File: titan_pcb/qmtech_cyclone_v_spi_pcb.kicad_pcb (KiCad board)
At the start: 2 copper layers, 146.1 x 95 mm, 47 parts, among them J1 FPGA, J10 OLED_CONN, J11 OLED_CONN, J12 CH341_PRG_CONN, J13 SPI_HEADER, J14 SPI_HEADER, J15 I2C_PULLUP, J16 I2C_PULLUP, J17 I2C_PULLUP, J18 I2C_PULLUP, J19 Barrel_Jack_MountingPin, J2 FPGA, J20 PWR_SW, J21 PWR_SW, J22 PWR_SW, J23 PWR_SW, J3 TEENSY, J4 TEENSY, J5 ESP, J6 ESP, J7 PICO, J8 PICO, J9 OLED_JMP, U1 LM1084-3.3

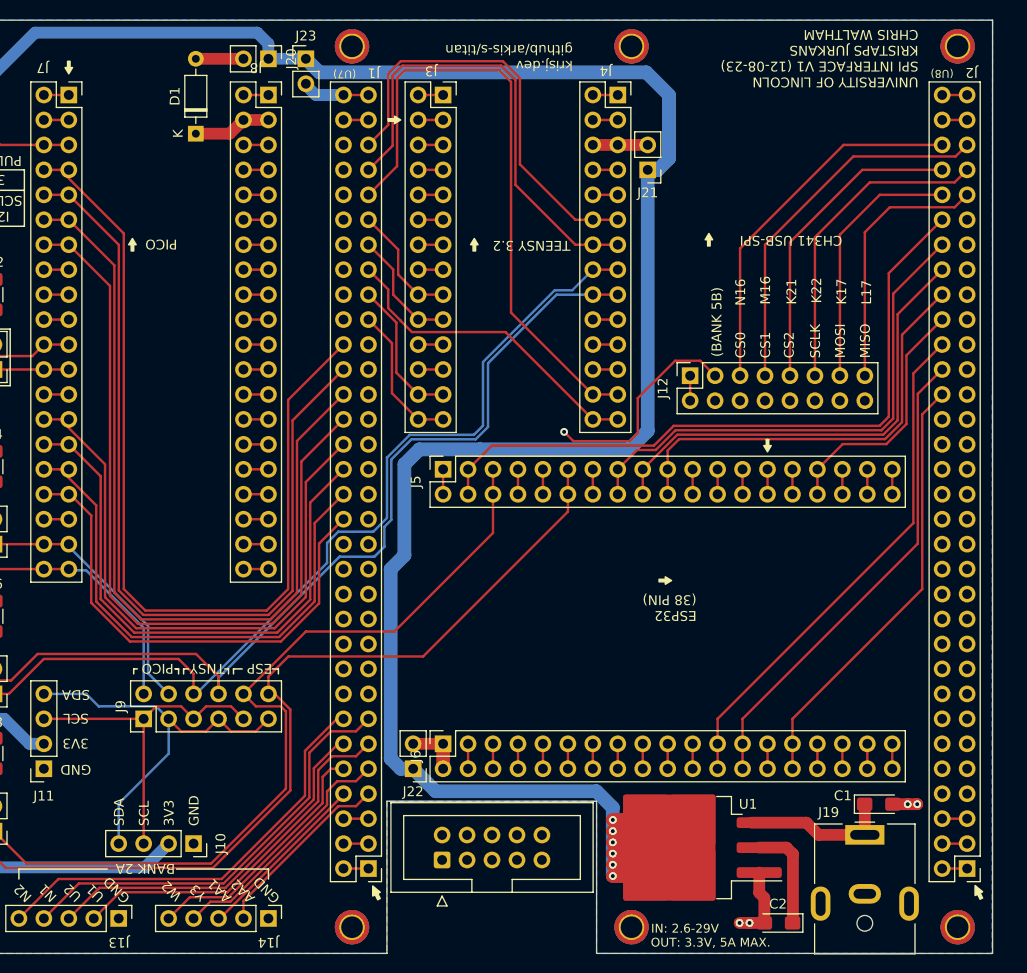
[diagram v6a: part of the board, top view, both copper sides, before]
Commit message: updated silkscreen
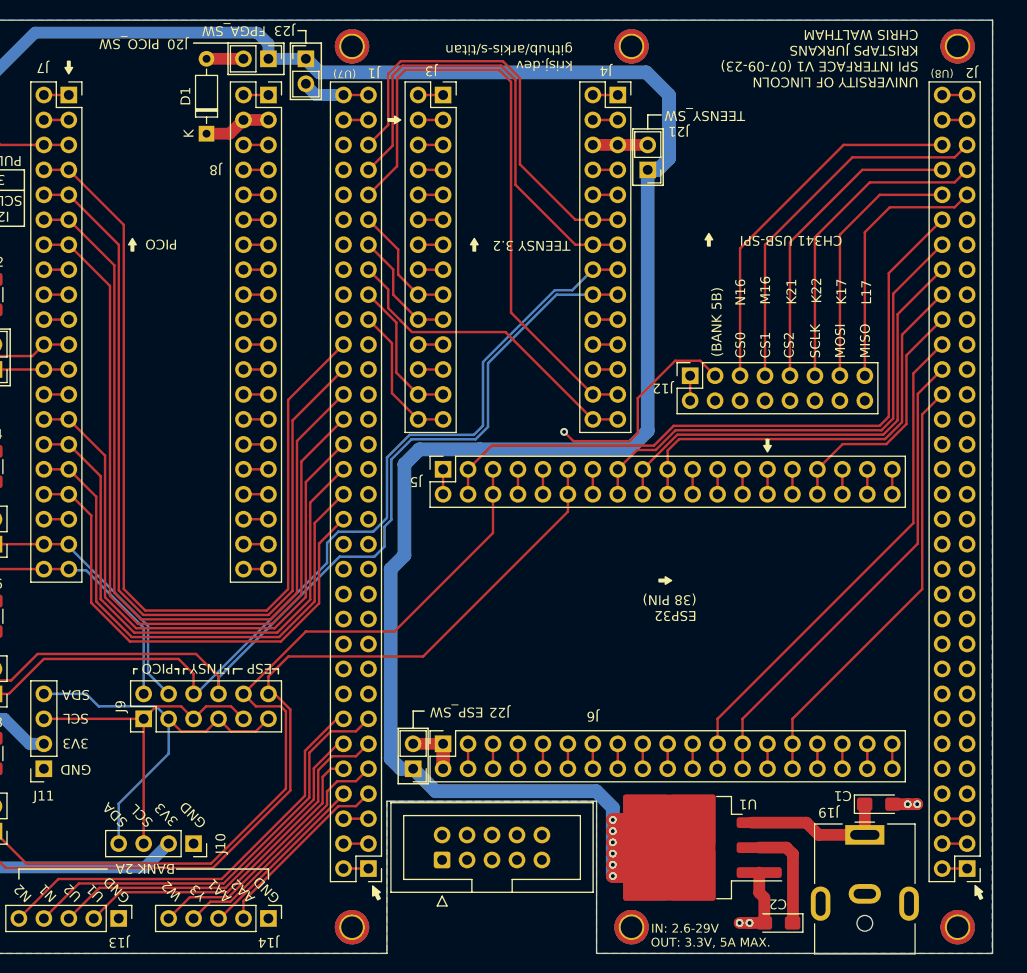
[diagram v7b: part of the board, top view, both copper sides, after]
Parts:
- moved D1 1.09 mm to (72.4, 42.0)
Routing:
- net PICO_VSYS: track 7.97 -> 6.88 mm
- net Net-(D1-A): track 4.85 -> 3.76 mm
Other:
- board text added: "ESP_SW"
- board text added: "FPGA_SW"
- board text added: "PICO_SW"
- board text added: "TEENSY_SW"
- board text added: "UNIVERSITY OF LINCOLN SPI INTERFACE V1 (07-09-23) KRISTAPS JURKANS CHRIS WALTHAM"
- board text removed: "UNIVERSITY OF LINCOLN SPI INTERFACE V1 (12-08-23) KRISTAPS JURKANS CHRIS WALTHAM"

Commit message: removed mcus, updated silkscreen, regenerated bom
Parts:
- removed UX1: ESP32-DevKitC, PCM_Espressif:ESP32-DevKitC
- removed UX2: Teensy3.2, teensy:Teensy30_31_32_LC
- removed UX3: Pico, MCU_RaspberryPi_and_Boards:RPi_Pico_SMD_TH
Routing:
- net BANK_8A_F10: track 94.2 -> 93.3 mm
- net BANK_8A_D9: track 55.4 -> 54.5 mm
- net BANK_8A_B7: track 63.2 -> 62.4 mm
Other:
- board text added: "UNIVERSITY OF LINCOLN SPI INTERFACE V1 (09-09-23) KRISTAPS JURKANS CHRIS WALTHAM"
- board text removed: "TODO: - ESP power supply?"
- board text removed: "UNIVERSITY OF LINCOLN SPI INTERFACE V1 (07-09-23) KRISTAPS JURKANS CHRIS WALTHAM"
